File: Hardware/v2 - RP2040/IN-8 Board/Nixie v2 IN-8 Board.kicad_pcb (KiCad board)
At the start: 2 copper layers, 100 x 75 mm, 41 parts, among them J1 Conn_01x10_Pin, J2 Conn_01x10_Pin, J3 Conn_01x10_Pin, J4 Conn_02x02_Odd_Even, Q1 MMBTA42, Q2 PZTA92, U1 NCH8200HV, U2 VEML7700, U3 К155ИД1, U4 К155ИД1, U5 К155ИД1, U6 К155ИД1

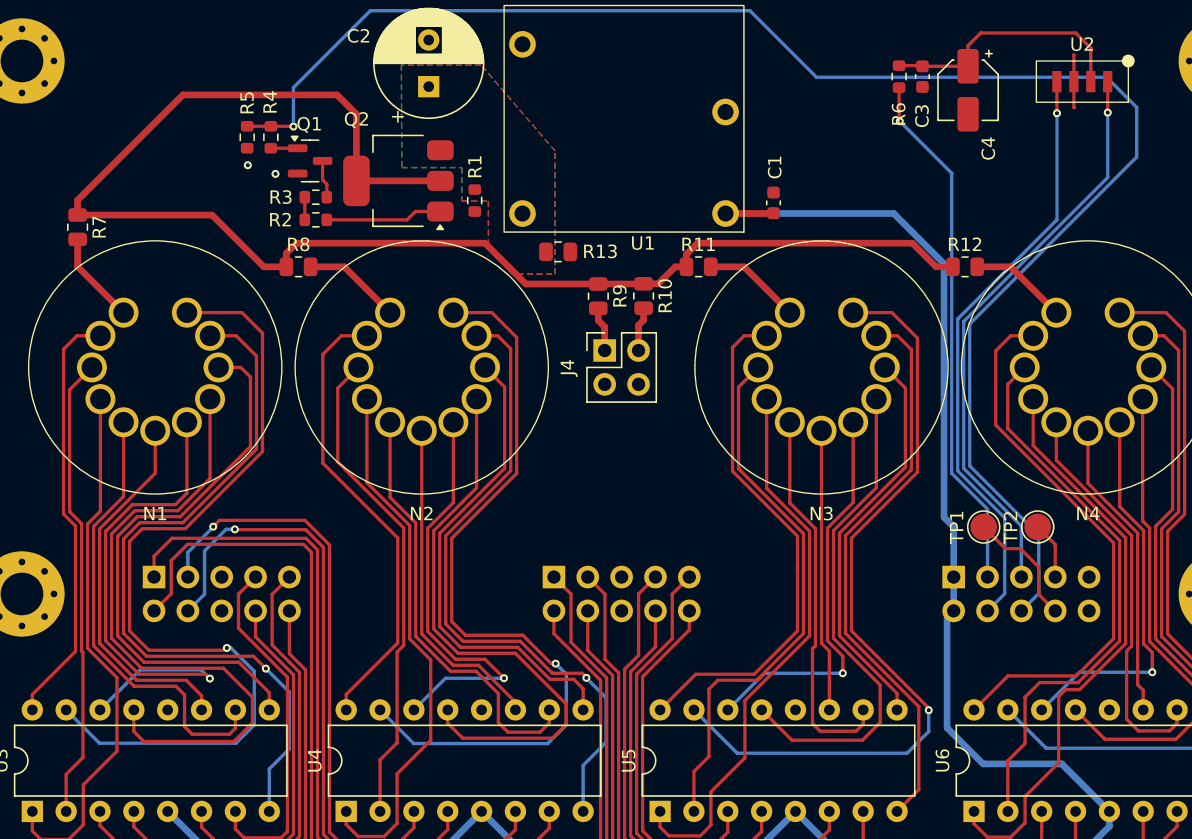
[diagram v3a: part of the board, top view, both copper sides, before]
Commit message: finished initial layout and swapped SDA/SCL on connector
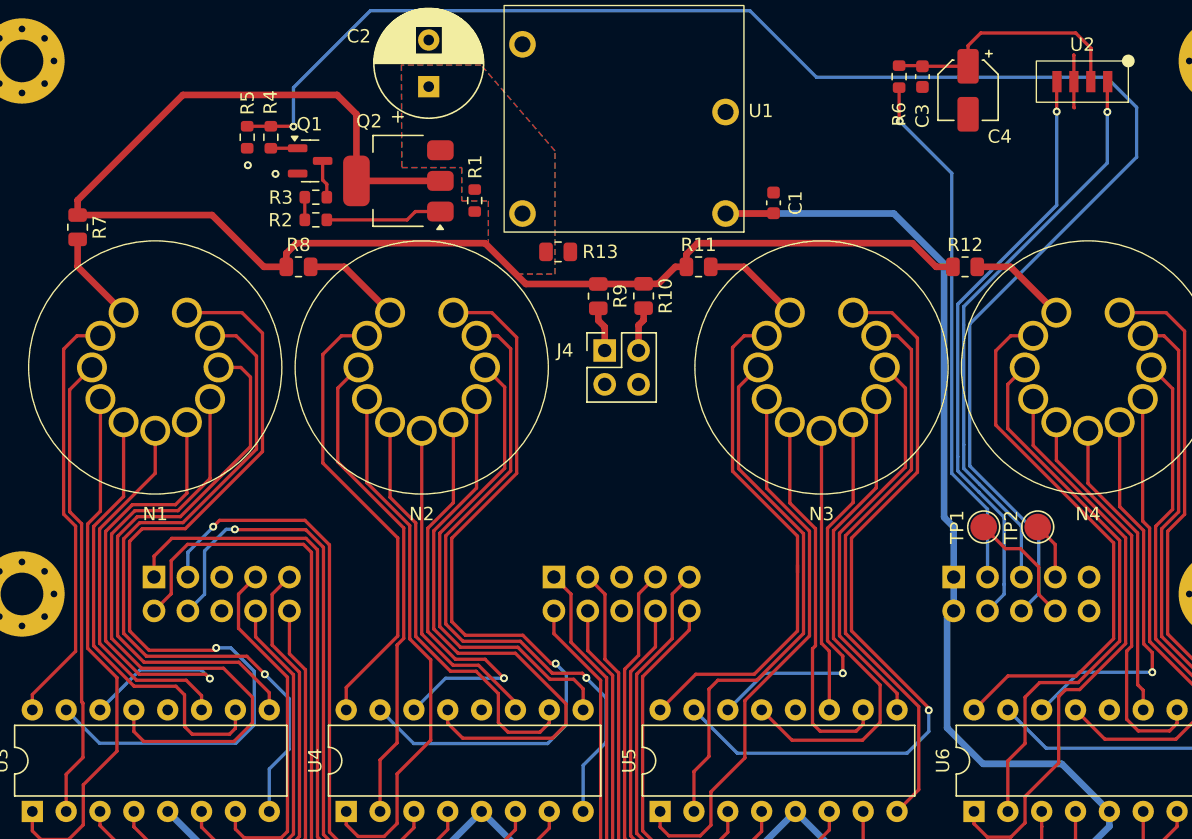
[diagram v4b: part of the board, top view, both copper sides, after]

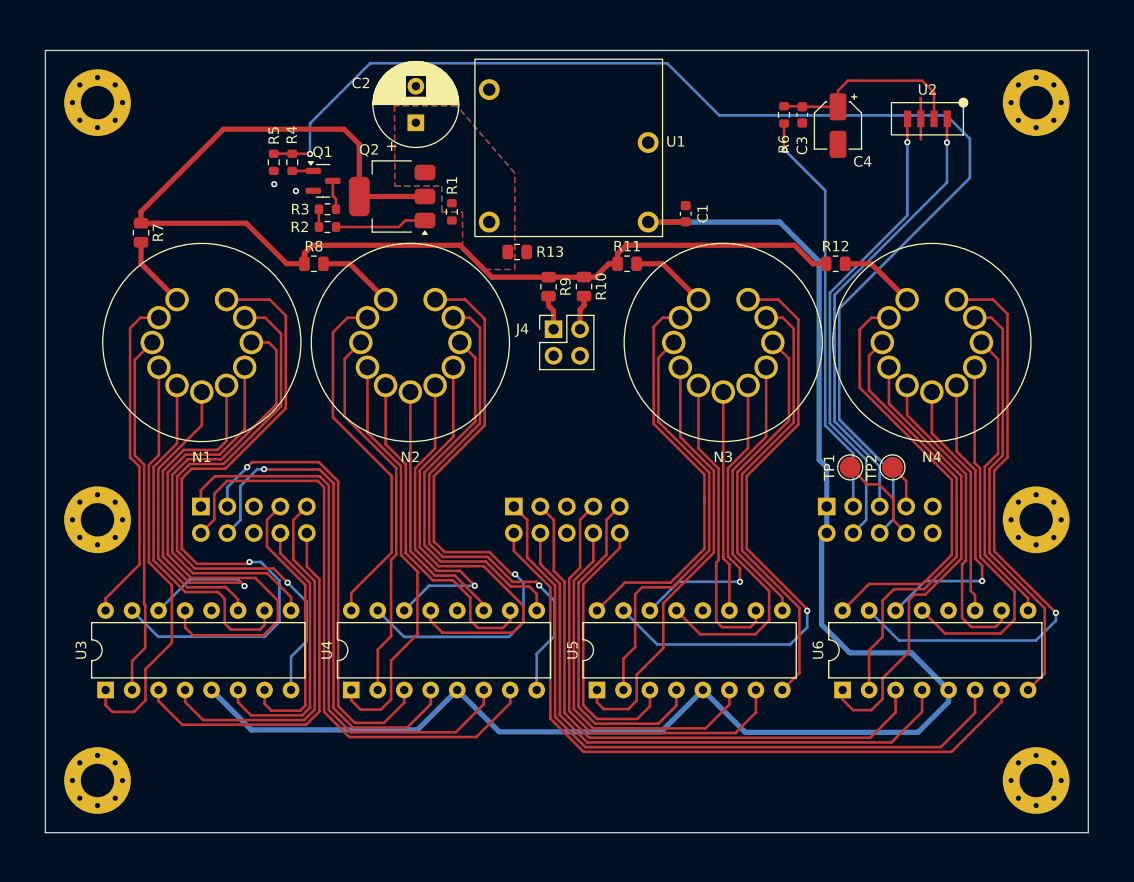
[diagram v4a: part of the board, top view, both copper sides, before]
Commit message: added ground via stitching, and baord names, version, designer, and date to silkscreen
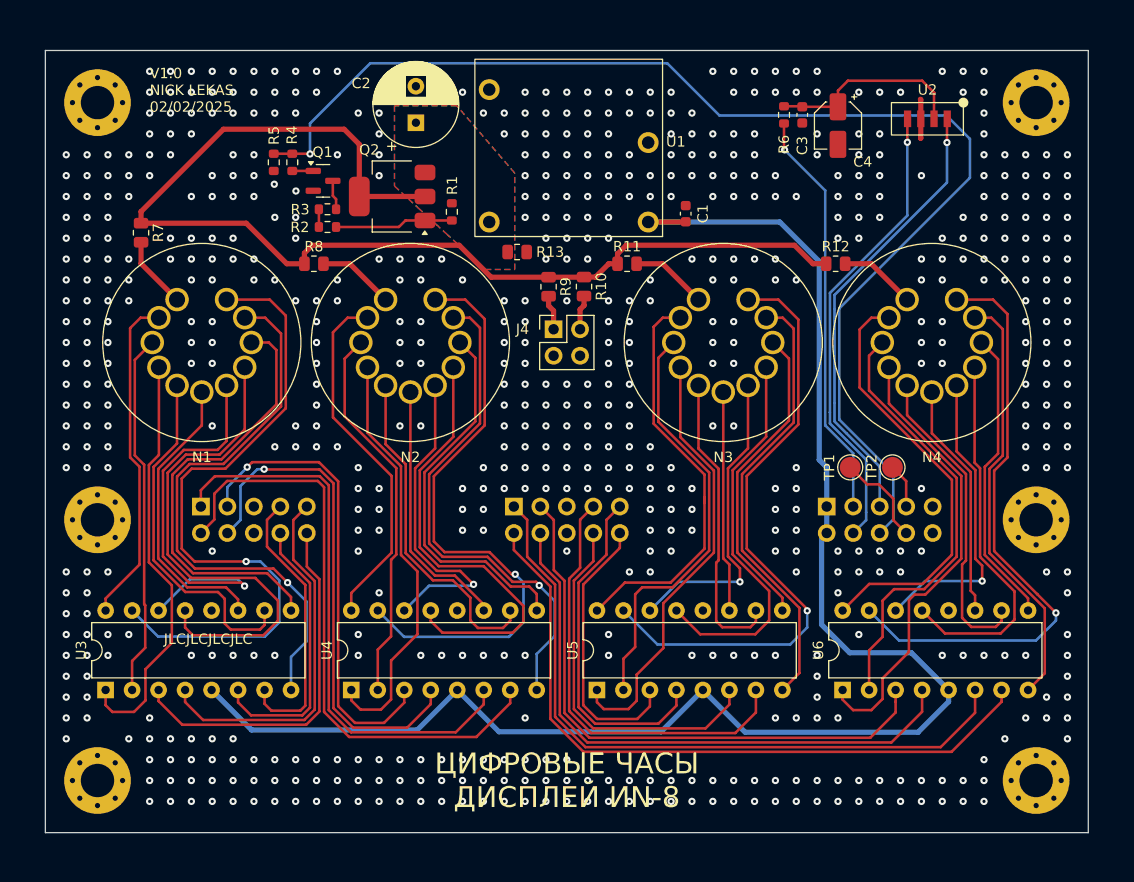
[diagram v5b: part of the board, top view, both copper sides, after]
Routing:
- net Net-(Q2-B): track 8.78 -> 11.4 mm
- net GND: track 4.00 -> 3.77 mm, vias 2 -> 666
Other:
- board text added: "JLCJLCJLCJLC"
- board text added: "V1.0 NICK LEKAS 02/02/2025"
- board text added: "ЦИФРОВЫЕ ЧАСЫ ДИСПЛЕЙ ИN-8"
